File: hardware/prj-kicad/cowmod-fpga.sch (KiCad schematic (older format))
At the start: 6 parts, among them U2 ICE40HX1K-TQ144

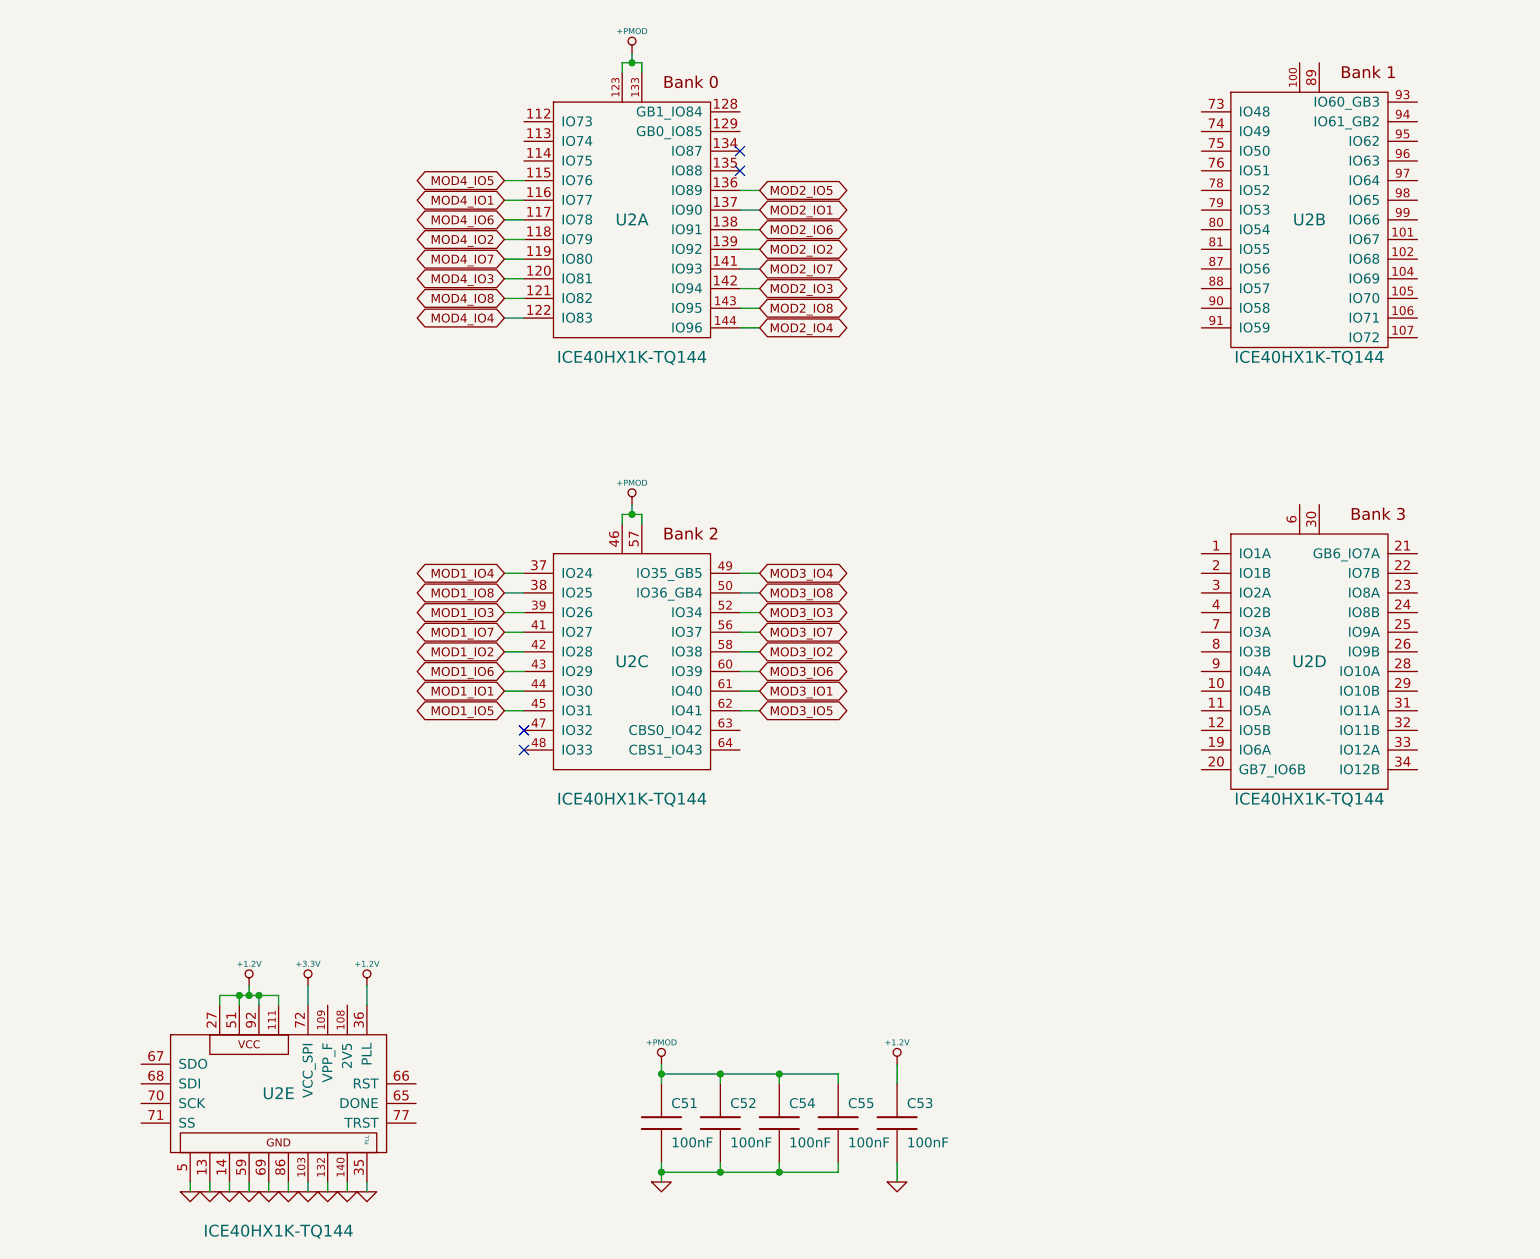
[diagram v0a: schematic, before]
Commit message: = ADD: Insert main MCU (STM32) and connect it to FPGA
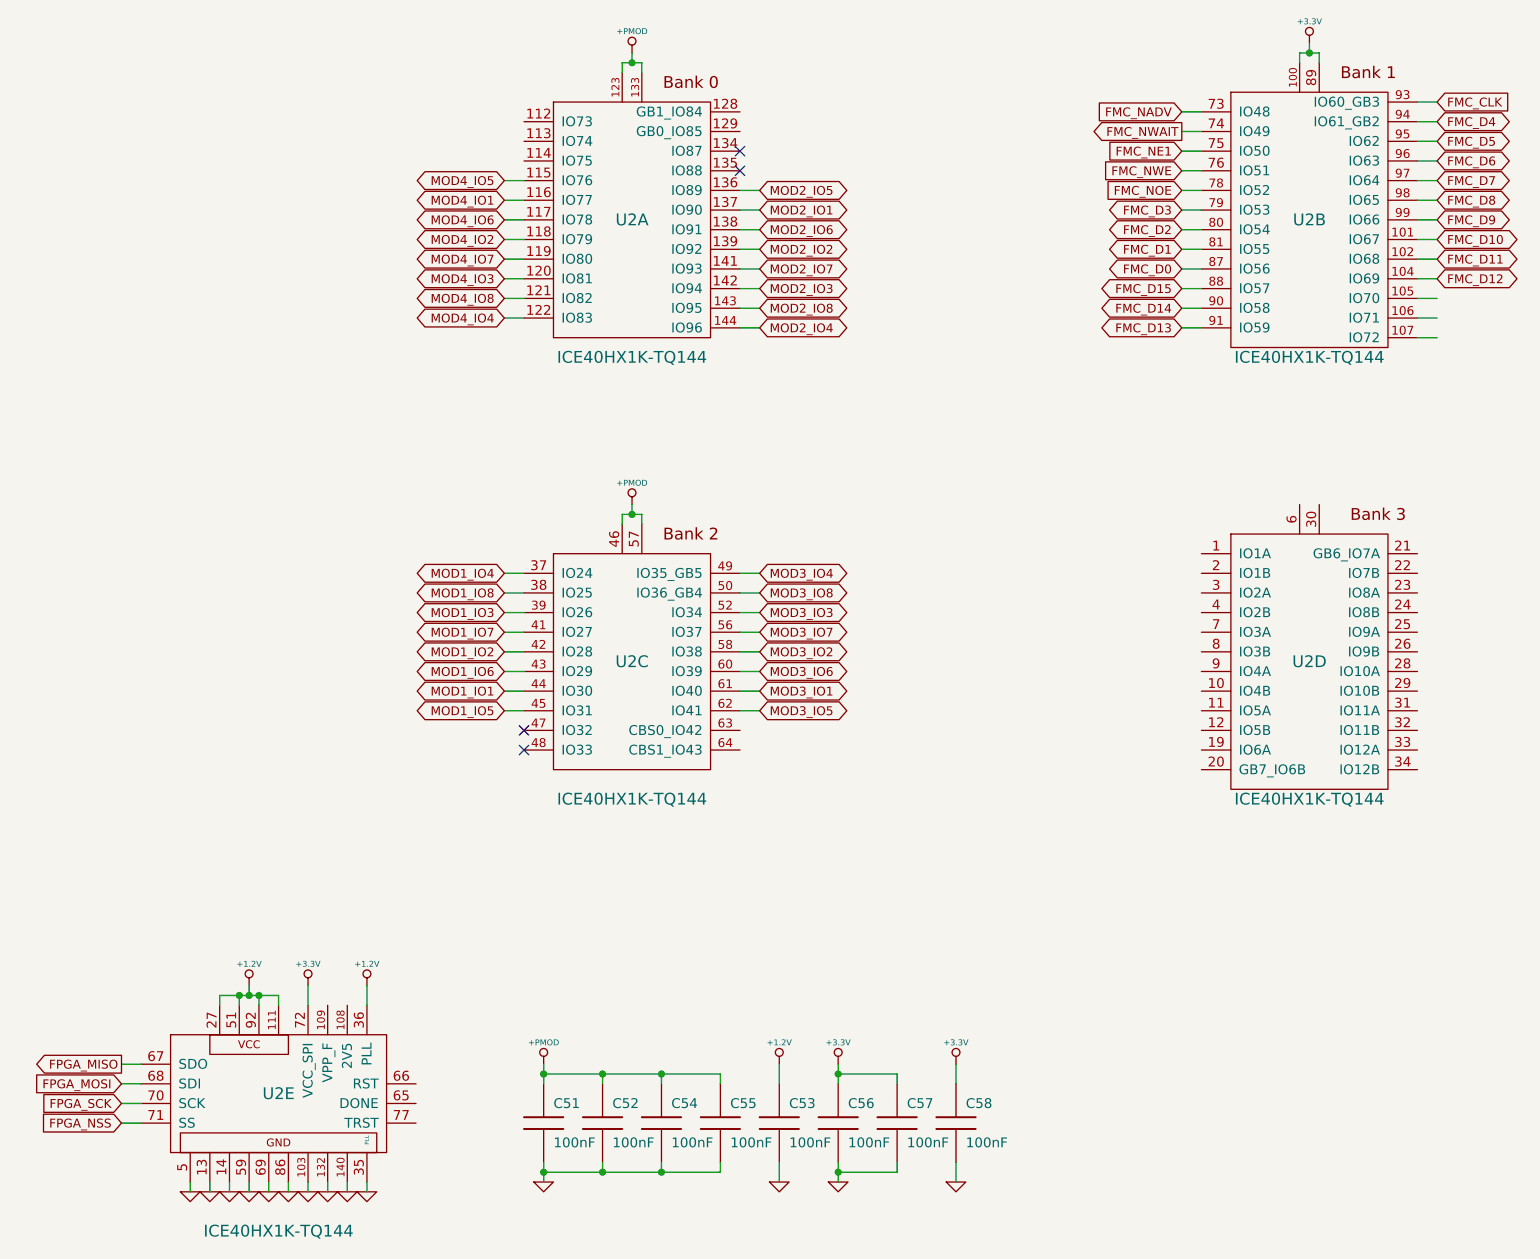
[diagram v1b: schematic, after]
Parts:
- added C56, C57, C58: 100nF, cowmod:SMD0603, symbol C
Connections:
- net +3.3V: now also U2.100, U2.89, C56.1, C57.1, C58.1
- net GND: now also C56.2, C57.2, C58.2
- net FMC_D10: now reaches U2.101 (IO67)
- net FMC_D11: now reaches U2.102 (IO68)
- net FMC_D12: now reaches U2.104 (IO69)
- net FMC_NADV: now reaches U2.73 (IO48)
- net FMC_NWAIT: now reaches U2.74 (IO49)
- net FMC_NE1: now reaches U2.75 (IO50)
- net FMC_NWE: now reaches U2.76 (IO51)
- net FMC_NOE: now reaches U2.78 (IO52)
- net FMC_D3: now reaches U2.79 (IO53)
- net FMC_D2: now reaches U2.80 (IO54)
- net FMC_D1: now reaches U2.81 (IO55)
- net FMC_D0: now reaches U2.87 (IO56)
- net FMC_D15: now reaches U2.88 (IO57)
- net FMC_D14: now reaches U2.90 (IO58)
- net FMC_D13: now reaches U2.91 (IO59)
- net FMC_CLK: now reaches U2.93 (IO60_GB3)
- net FMC_D4: now reaches U2.94 (IO61_GB2)
- net FMC_D5: now reaches U2.95 (IO62)
- net FMC_D6: now reaches U2.96 (IO63)
- net FMC_D7: now reaches U2.97 (IO64)
- net FMC_D8: now reaches U2.98 (IO65)
- net FMC_D9: now reaches U2.99 (IO66)
- net FPGA_MISO: now reaches U2.67 (SDO)
- net FPGA_MOSI: now reaches U2.68 (SDI)
- net FPGA_SCK: now reaches U2.70 (SCK)
- net FPGA_NSS: now reaches U2.71 (SS)
